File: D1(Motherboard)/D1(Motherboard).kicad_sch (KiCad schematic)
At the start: 72 parts, among them J1 WR-FPC_0.5mm_ZIF_V, J2 USB_C_Receptacle_USB2.0, J3 B2B-PH-K-S, Q1 NX2301P.215, SW1 CHS-02A, U2 ICM-20602, U3 WR-FPC_0.5mm_ZIF_H, U4 MIC5353-3.3YMT, U5 FAN5331SX, U6 MCP73831-2-OT

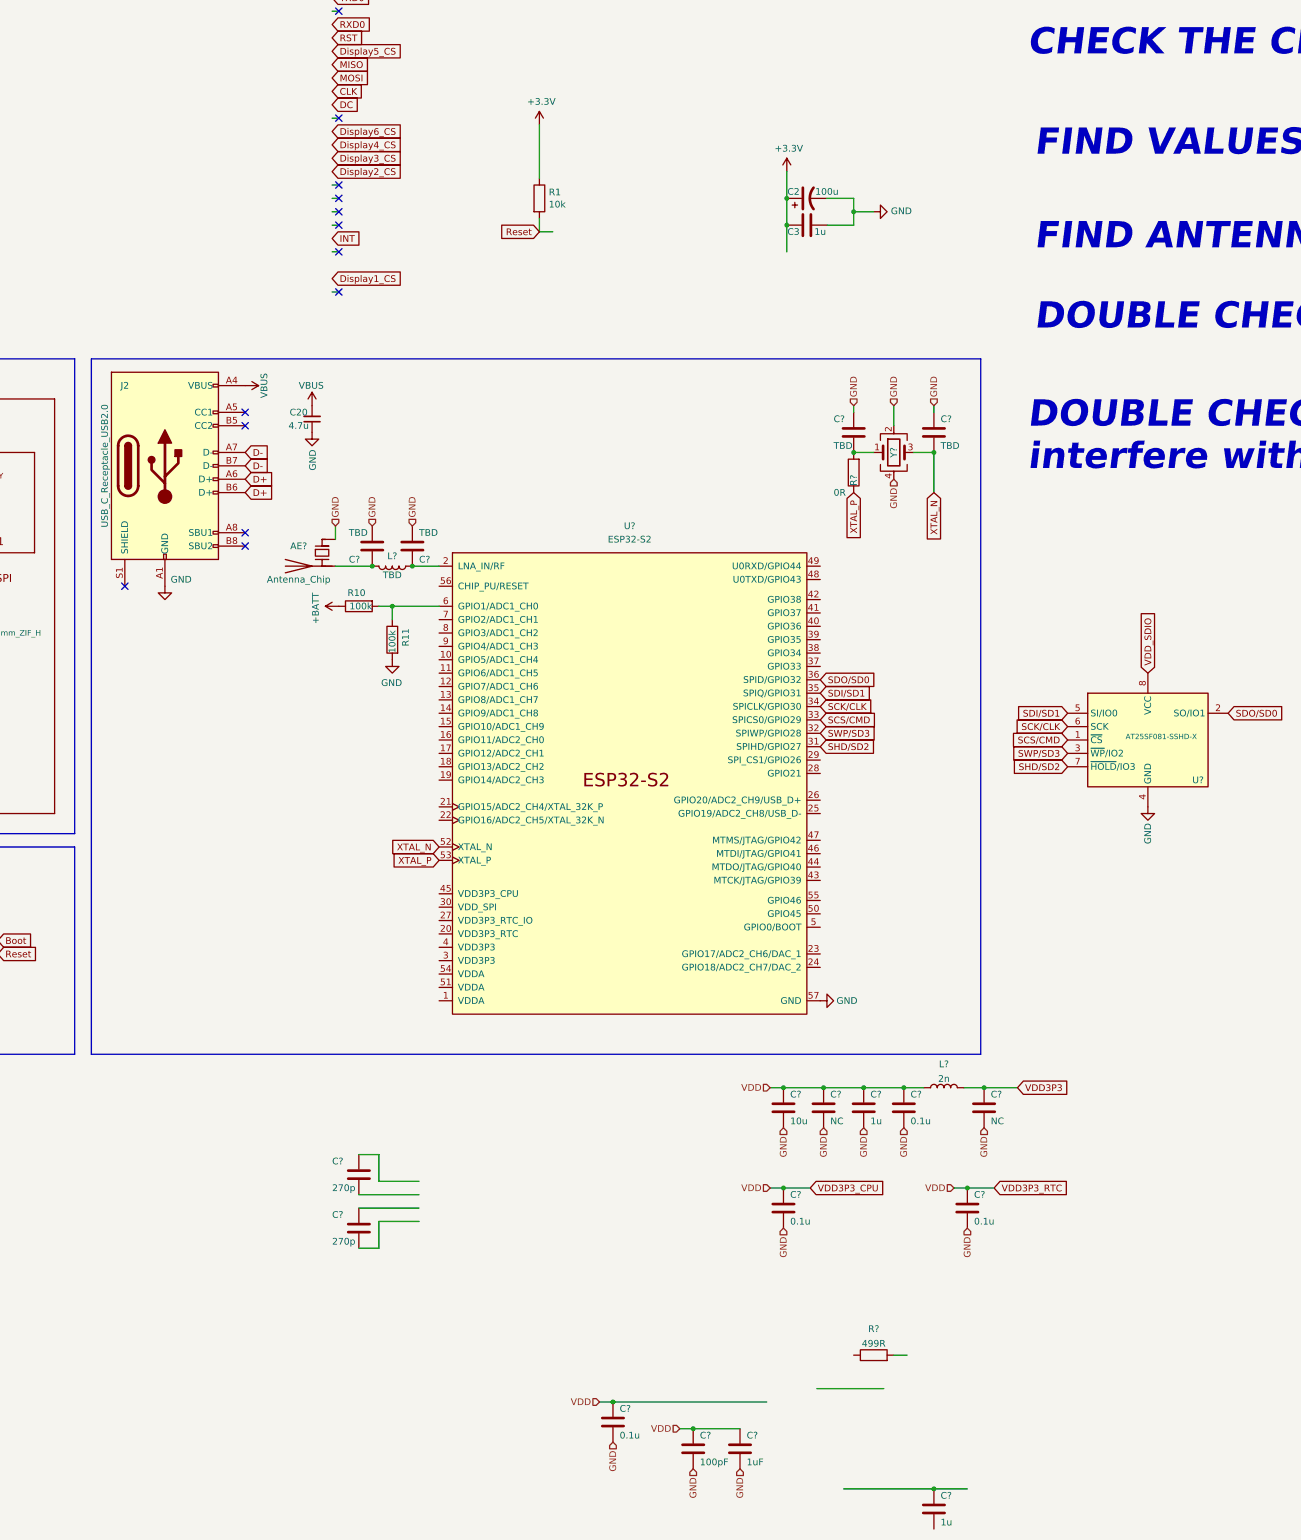
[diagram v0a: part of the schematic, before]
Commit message: Fixed ignion antenna, and added some more to the esp32-s2 schematic
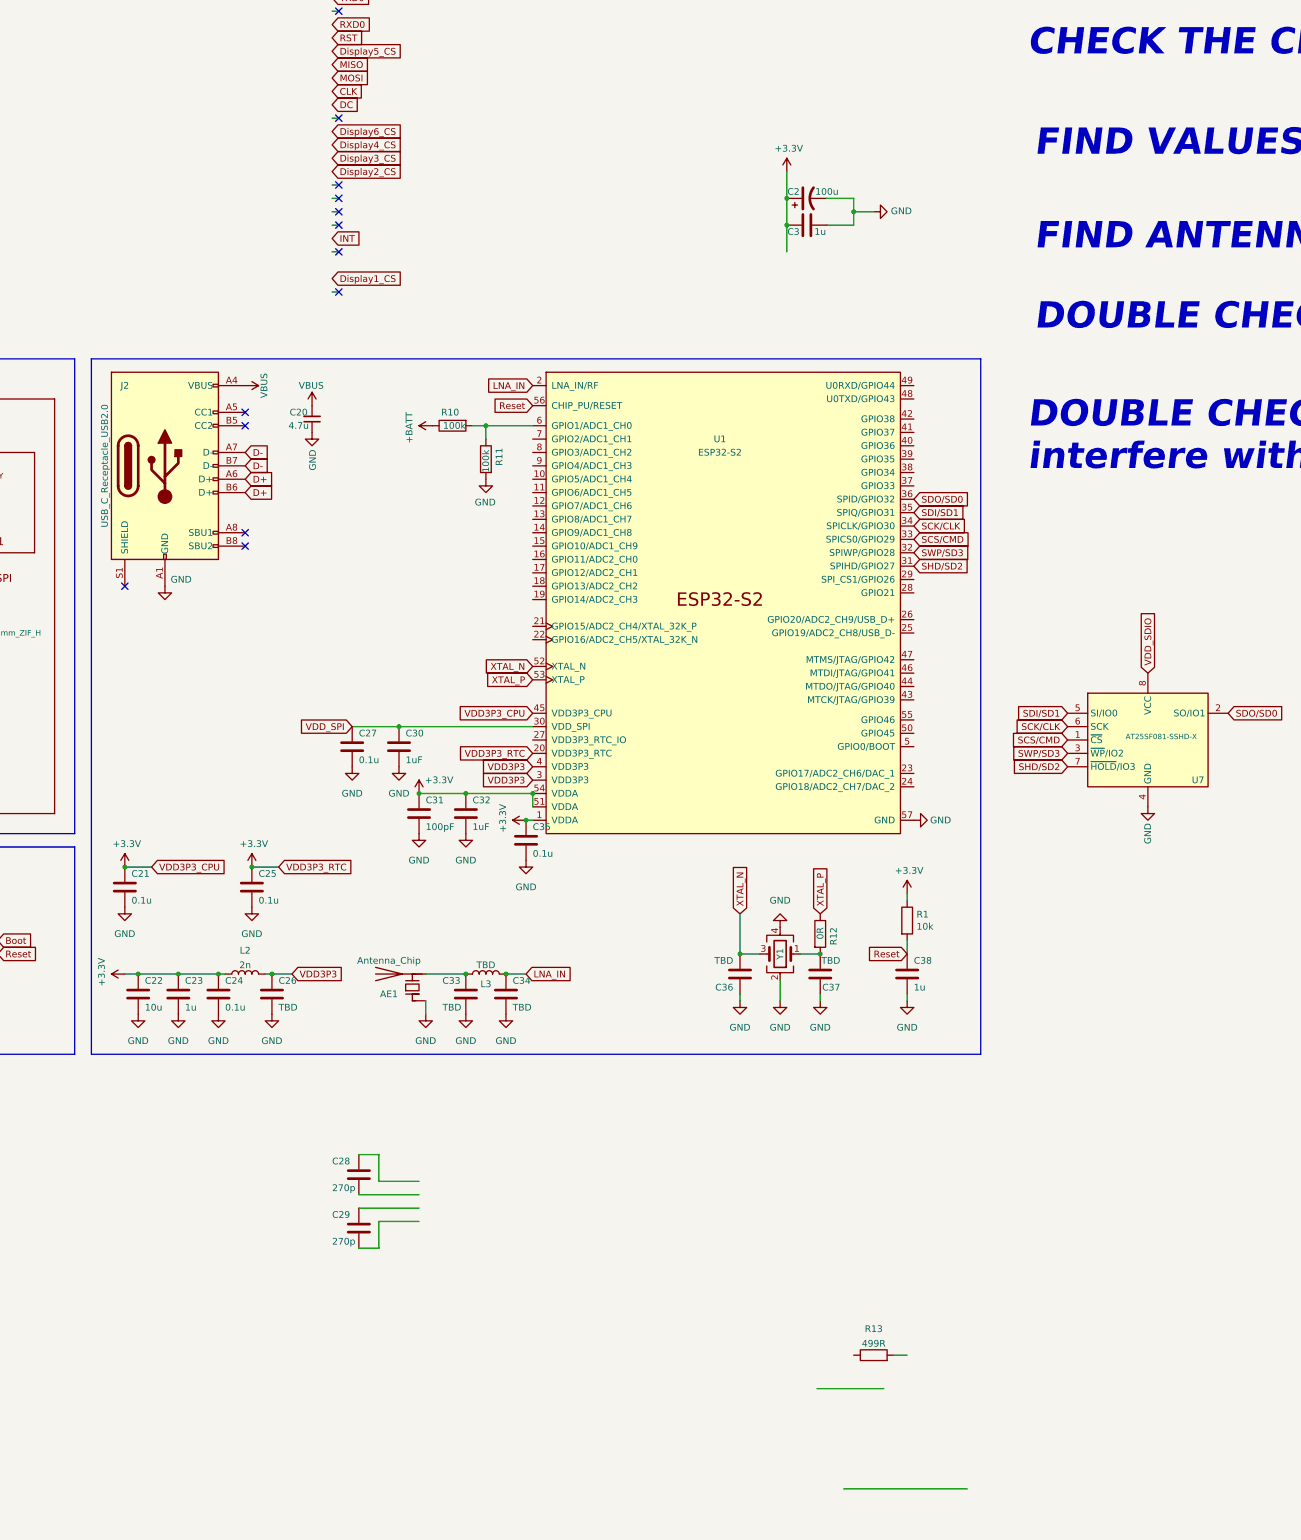
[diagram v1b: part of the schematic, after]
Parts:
- removed C?: NC, Capacitor_SMD:C_0603_1608Metric, symbol Device:C
- added C27: 0.1u, Capacitor_SMD:C_0603_1608Metric, symbol Device:C
- added C30: 1uF, Capacitor_SMD:C_0603_1608Metric, symbol Device:C
- AE1: renamed from AE?; footprint Ignion_Antenna:NN03-320 -> Ignion_Antenna:NN02-101
- C26: renamed from C?; value NC -> TBD
- gave numbers to parts that had none: 22
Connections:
- net VDD3P3_CPU is gone; now on net +3V3: C21.1, C22.1, C23.1, C24.1, C25.1, C31.1, C32.1, C35.1, L2.1
- net +3V3: now also U1.1 (VDDA), U1.20 (VDD3P3_RTC), U1.45 (VDD3P3_CPU), U1.51 (VDDA), U1.54 (VDDA)
- net GND: now also C38.2, C27.2, C30.2
- net Reset: now also C38.1, U1.56 (CHIP_PU/RESET)
- net VDD3P3: now also U1.3 (VDD3P3), U1.4 (VDD3P3)
- net LNA_IN: now reaches C34.1, L3.2, U1.2 (LNA_IN/RF)
- net VDD_SPI: now reaches U1.30 (VDD_SPI)
- net VDD_SPI: now also C27.1, C30.1
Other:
- moved on the sheet: AE1, C21, C22, C23, C24, C25, C26, C31, C32, C33, C34, C35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

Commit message: Added Flash memory, is it worth adding PSRAM???
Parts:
- removed C29: 270p, Capacitor_SMD:C_0603_1608Metric, symbol Device:C
- removed U7: AT25SF081-SSHD-X, Package_SO:SOIC-8_3.9x4.9mm_P1.27mm, symbol Memory_Flash:AT25SF081-SSHD-X
- added R14: 10k(NC), Resistor_SMD:R_0603_1608Metric, symbol Device:R
- added U7: W25Q128JVS, Package_SO:SOIC-8_5.23x5.23mm_P1.27mm, symbol Memory_Flash:W25Q128JVS
- C28: value 270p -> 0.1u
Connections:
- net GND: now also C28.2, U7.4 (GND)
- net VDD_SPI: now also C28.1, R14.1, U7.8 (VCC)
- net at U1.48 (U0TXD/GPIO43): now also R13.1
- net U0RXD: now reaches U1.49 (U0RXD/GPIO44)
- net U0TXD: now reaches R13.2
- net SCK/CLK renamed SPICLK
- net SCS/CMD renamed SPICS0
- net SPICS0: now also R14.2, U7.1 (~{CS}), U7.6 (CLK)
- net SDI/SD1 renamed SPIQ
- net SPIQ: now also U7.2 (DO(IO1))
- net SDO/SD0 renamed SPID
- net SPID: now also U7.5 (DI(IO0))
- net SHD/SD2 renamed SPIHD
- net SPIHD: now also U7.7 (IO3)
- net SWP/SD3 renamed SPIWP
- net SPIWP: now also U7.3 (IO2)
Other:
- note removed: "DONT HAVE ICM20602"
- moved on the sheet: AE1, C20, C21, C25, C27, C30, C31, C32, C33, C34, C35, C36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

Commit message: Sorted out antenna + setout loctions in corner
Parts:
- removed R12: 0R, Resistor_SMD:R_0603_1608Metric, symbol Device:R
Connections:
- net SPICLK: now also U7.6 (CLK)
- net SPICS0: no longer U7.6 (CLK)
- net XTAL_P: now also C37.2, Y1.1
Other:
- note added: "IS ZERO OHM RESISTOR NEEDED FOR THE CRYSTAL???"
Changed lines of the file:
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@@
   (junction (at 180.975 151.13) (diameter 0) (color 0 0 0 0)
   )
-  (junction (at 269.24 87.63) (diameter 0) (color 0 0 0 0)
-  )
   (junction (at 269.24 184.15) (diameter 0) (color 0 0 0 0)
   )
@@
   (junction (at 377.19 41.91) (diameter 0) (color 0 0 0 0)
   )
+  (junction (at 269.24 87.63) (diameter 0) (color 0 0 0 0)
+  )
   (junction (at 19.05 88.9) (diameter 0) (color 0 0 0 0)
   )
@@
     (stroke (width 0) (type default) (color 0 0 0 0))
   )
+  (wire (pts (xy 269.24 80.01) (xy 269.24 87.63))
+    (stroke (width 0) (type default) (color 0 0 0 0))
+  )
   (wire (pts (xy 192.405 80.01) (xy 200.025 80.01))
     (stroke (width 0) (type default) (color 0 0 0 0))
@@
     (effects (font (size 5 5) (thickness 1) bold italic) (justify left bottom))
   )
+  (text "IS ZERO OHM RESISTOR NEEDED FOR THE CRYSTAL???" (at 469.9 165.1 0)
+    (effects (font (size 5 5) (thickness 1) bold italic) (justify left bottom))
+  )
   (text "All Parts Aquired" (at 90.805 127 0)
     (effects (font (size 1.27 1.27)) (justify left bottom))
@@
     )
   )
+  (global_label "SPICLK" (shape input) (at 354.33 185.42 180) (fields_autoplaced)
+    (effects (font (size 1.27 1.27)) (justify right))
+    (property "Intersheet References" "${INTERSHEET_REFS}" (id 0) (at 345.3534 185.4994 0)
+      (effects (font (size 1.27 1.27)) (justify right) hide)
+    )
+  )
   (global_label "MOSI" (shape input) (at 200.025 107.95 180) (fields_autoplaced)
     (effects (font (size 1.27 1.27)) (justify right))
@@
     )
   )
-  (global_label "SPICS0" (shape input) (at 354.33 185.42 180) (fields_autoplaced)
-    (effects (font (size 1.27 1.27)) (justify right))
-    (property "Intersheet References" "${INTERSHEET_REFS}" (id 0) (at 345.2325 185.4994 0)
-      (effects (font (size 1.27 1.27)) (justify right) hide)
-    )
-  )
   (global_label "RXD0" (shape input) (at 290.83 3.81 0) (fields_autoplaced)
     (effects (font (size 1.27 1.27)) (justify left))
@@
     (pin "1")
   )
-  (symbol (lib_id "Device:R") (at 269.24 83.82 0) (unit 1)
-    (in_bom yes) (on_board yes)
-    (property "Reference" "R12" (id 0) (at 271.78 82.55 90)
-      (effects (font (size 1.27 1.27)) (justify right))
-    )
-    (property "Value" "0R" (id 1) (at 269.24 82.55 90)
-      (effects (font (size 1.27 1.27)) (justify right))
-    )
-    (property "Footprint" "Resistor_SMD:R_0603_1608Metric" (id 2) (at 267.462 83.82 90)
-      (effects (font (size 1.27 1.27)) hide)
-    )
-    (property "Datasheet" "~" (id 3) (at 269.24 83.82 0)
-      (effects (font (size 1.27 1.27)) hide)
-    )
-    (pin "1")
-    (pin "2")
-  )
   (symbol (lib_id "power:GND") (at 261.62 82.55 180) (unit 1)
     (in_bom yes) (on_board yes)
@@
       (reference "R11") (unit 1) (value "100k") (footprint "Resistor_SMD:R_0603_1608Metric")
     )
-    (path "/fa505ada-ba55-42ef-84ac-b3a5b07dba31"
-      (reference "R12") (unit 1) (value "0R") (footprint "Resistor_SMD:R_0603_1608Metric")
-    )
     (path "/c0639a7b-dbec-4037-b44c-e481467478f8"

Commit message: Fixed 3D Models etc, and added to schematics + PCB
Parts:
- added C?: 0.1u, Capacitor_SMD:C_0603_1608Metric, symbol Device:C
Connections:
- net +3V3: now also U1.27 (VDD3P3_RTC_IO), C?.1
- net Boot: now also U1.5 (GPIO0/BOOT)
- net CLK: now also U1.40 (GPIO36)
- net D+: now also U1.26 (GPIO20/ADC2_CH9/USB_D+)
- net D-: now also U1.25 (GPIO19/ADC2_CH8/USB_D-)
- net Display1_CS: now also U1.19 (GPIO14/ADC2_CH3)
- net Display2_CS: now also U1.18 (GPIO13/ADC2_CH2)
- net Display3_CS: now also U1.17 (GPIO12/ADC2_CH1)
- net Display4_CS: now also U1.16 (GPIO11/ADC2_CH0)
- net Display6_CS: now also U1.15 (GPIO10/ADC1_CH9)
- net GND: now also C?.2
- net MISO: now also U1.41 (GPIO37)
- net MOSI: now also U1.39 (GPIO35)
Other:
- note added: "DO THE CC PINS ON USB NEED TO BE INCLUDED?"
- note added: "GO THROUGH THE HARDWARE DESIGN GUIDES TO SEE IF ALL ASPECTS ARE VALID"
- note added: "HOW MUCH VOLTAGE/CURRENT CAN THE ANALOG PINS TAKE FROM THE BATTERRY TO MEASURE CAPACITY"
- note removed: "MOVE BATTERY VOLTAGE PIN AROUND TO BEST POSITION"
- note removed: "TRIPLE CHECK THE CORRECT REFERENCES FOR LOAD SHARING CIRCUIT! LOOKS WRONG FROM FIRST GLANCE WITH 5V, VBUS AND VBAT"
- moved on the sheet: AE1, C20, C21, C22, C23, C24, C25, C26, C27, C28, C30, C33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

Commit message: More PCB work
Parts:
- removed C2: 100u, Capacitor_Tantalum_SMD:CP_EIA-3216-18_Kemet-A, symbol Device:CP1
- removed C3: 1u, Capacitor_SMD:C_0603_1608Metric, symbol Device:C
- gave numbers to parts that had none: 1
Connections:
- net Display1_CS: now also U1.14 (GPIO9/ADC1_CH8); no longer U1.19 (GPIO14/ADC2_CH3)
- net Display2_CS: now also U1.15 (GPIO10/ADC1_CH9); no longer U1.18 (GPIO13/ADC2_CH2)
- net Display3_CS: now also U1.16 (GPIO11/ADC2_CH0); no longer U1.17 (GPIO12/ADC2_CH1)
- net Display4_CS: now also U1.17 (GPIO12/ADC2_CH1); no longer U1.16 (GPIO11/ADC2_CH0)
- net Display5_CS: now also U1.18 (GPIO13/ADC2_CH2)
- net Display6_CS: now also U1.19 (GPIO14/ADC2_CH3); no longer U1.15 (GPIO10/ADC1_CH9)
- no-connect marks 17 -> 11
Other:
- note added: "ADD INTERNAL LED TO USE AS HELLO WORLD"
- note added: "WHERE SHOULD DC, INT AND RST GO"
- moved on the sheet: AE1, C2, C21, C22, C23, C24, C25, C26, C27, C30, C31, C32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

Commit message: Changed antenna symbol and removed ground from pin + more layout
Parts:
- removed AE1: Antenna_Chip, Ignion_Antenna:NN02-101, symbol Device:Antenna_Chip
- added Reference1: Ignion-NN02-101, Ignion_Antenna:NN02-101, symbol Device:Antenna
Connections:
- net at C33.1, L3.1: now also Reference1.1 (A)
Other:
- note added: "WHAT ARE YOU MEANT TO DO WITH PINS OF ANTENNA?"
- note removed: "FIND ANTENNA"
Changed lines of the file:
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@@
     (stroke (width 0) (type default) (color 0 0 0 0))
   )
-  (wire (pts (xy 262.89 109.22) (xy 262.89 111.76))
-    (stroke (width 0) (type default) (color 0 0 0 0))
-  )
   (polyline (pts (xy 154.94 121.92) (xy 154.94 67.31))
     (stroke (width 0) (type default) (color 0 0 0 0))
@@
     (effects (font (size 5 5) (thickness 1) bold italic) (justify left bottom))
   )
-  (text "FIND ANTENNA" (at 422.91 45.72 0)
+  (text "WHAT ARE YOU MEANT TO DO WITH PINS OF ANTENNA?" (at 422.91 45.72 0)
     (effects (font (size 5 5) (thickness 1) bold italic) (justify left bottom))
   )
@@
     (pin "1")
   )
-  (symbol (lib_id "power:GND") (at 262.89 111.76 0) (unit 1)
-    (in_bom yes) (on_board yes)
-    (property "Reference" "#PWR0182" (id 0) (at 262.89 118.11 0)
-      (effects (font (size 1.27 1.27)) hide)
-    )
-    (property "Value" "GND" (id 1) (at 266.7 113.03 0))
-    (property "Footprint" "" (id 2) (at 262.89 111.76 0)
-      (effects (font (size 1.27 1.27)) hide)
-    )
-    (property "Datasheet" "" (id 3) (at 262.89 111.76 0)
-      (effects (font (size 1.27 1.27)) hide)
-    )
-    (pin "1")
-  )
   (symbol (lib_id "power:GND") (at 290.83 144.78 0) (unit 1)
     (in_bom yes) (on_board yes)
@@
     (pin "2")
   )
+  (symbol (lib_id "Device:Antenna") (at 257.81 104.14 90) (unit 1)
+    (in_bom yes) (on_board yes) (fields_autoplaced)
+    (property "Reference" "Reference1" (id 0) (at 258.445 97.79 90)
+      (effects (font (size 0 0)))
+    )
+    (property "Value" "Ignion-NN02-101" (id 1) (at 258.445 100.33 90))
+    (property "Footprint" "Ignion_Antenna:NN02-101" (id 2) (at 257.81 104.14 0)
+      (effects (font (size 1.27 1.27)) hide)
+    )
+    (property "Datasheet" "~" (id 3) (at 257.81 104.14 0)
+      (effects (font (size 1.27 1.27)) hide)
+    )
+    (pin "1")
+  )
   (symbol (lib_id "power:GND") (at 314.96 158.75 0) (unit 1)
     (in_bom yes) (on_board yes)
@@
     (pin "1")
   )
-  (symbol (lib_id "Device:Antenna_Chip") (at 260.35 106.68 90) (unit 1)
-    (in_bom yes) (on_board yes)
-    (property "Reference" "AE1" (id 0) (at 255.905 107.95 90))
-    (property "Value" "Antenna_Chip" (id 1) (at 255.905 101.6 90))
-    (property "Footprint" "Ignion_Antenna:NN02-101" (id 2) (at 255.905 109.22 0)
-      (effects (font (size 1.27 1.27)) hide)
-    )
-    (property "Datasheet" "~" (id 3) (at 255.905 109.22 0)
-      (effects (font (size 1.27 1.27)) hide)
-    )
-    (pin "1")
-    (pin "2")
-  )
   (symbol (lib_id "Device:C") (at 323.85 158.75 0) (unit 1)
     (in_bom yes) (on_board yes)
@@
       (reference "#PWR0181") (unit 1) (value "GND") (footprint "")
     )
-    (path "/7928e7e2-032f-4e20-b344-fe064441bbb3"
-      (reference "#PWR0182") (unit 1) (value "GND") (footprint "")
-    )
     (path "/ec4d5739-dd5c-4a57-b41b-4e6fbb6586f0"
       (reference "#PWR0183") (unit 1) (value "GND") (footprint "")
@@
       (reference "#U0104") (unit 1) (value "13V") (footprint "")
     )
-    (path "/cf43d2ad-dcbd-445a-a646-1fd9a722c52b"
-      (reference "AE1") (unit 1) (value "Antenna_Chip") (footprint "Ignion_Antenna:NN02-101")
-    )
     (path "/00000000-0000-0000-0000-00006168acd8"
       (reference "C1") (unit 1) (value "4.7u") (footprint "Capacitor_SMD:C_0603_1608Metric")
@@
       (reference "R14") (unit 1) (value "10k(NC)") (footprint "Resistor_SMD:R_0603_1608Metric")
     )
+    (path "/b0924ee8-742c-4c94-895d-32d756bc4fae"
+      (reference "Reference1") (unit 1) (value "Ignion-NN02-101") (footprint "Ignion_Antenna:NN02-101")
+    )
     (path "/00000000-0000-0000-0000-000060fd70d1"
